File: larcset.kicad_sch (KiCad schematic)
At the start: 246 parts, among them J1 EAR, J2 ANT, J3 MIC, J4 KEY, J6 Barrel_Jack_Switch, J7 FRONT_PANEL, J8 Conn_01x02, K1 G5V-2, Q1 MMBT2222A, Q10 MMBT2222A, Q11 2N7002, Q12 2N7002, Q13 2N3904, Q14 MMBT2222A, Q15 MMBT2222A, Q16 2N7002, Q17 2N7002, Q18 MMBT2222A, Q19 2N3904, Q2 MMBT2222A, Q20 2N7002, Q21 2N7002, Q22 IRF510N, Q3 MMBT2222A, Q4 MMBT2222A, Q5 MMBT2222A, Q6 MMBT2222A, Q7 MMBT2222A, Q8 MMBT2222A, Q9 MMBT2222A, T1 TRIFILAR_XFRMR, T2 TRIFILAR_XFRMR, T3 TRIFILAR_XFRMR, U1 LM386, Y1 11.059M, Y2 11.059M, Y3 11.059M, Y4 11.059M, Y5 11.059M

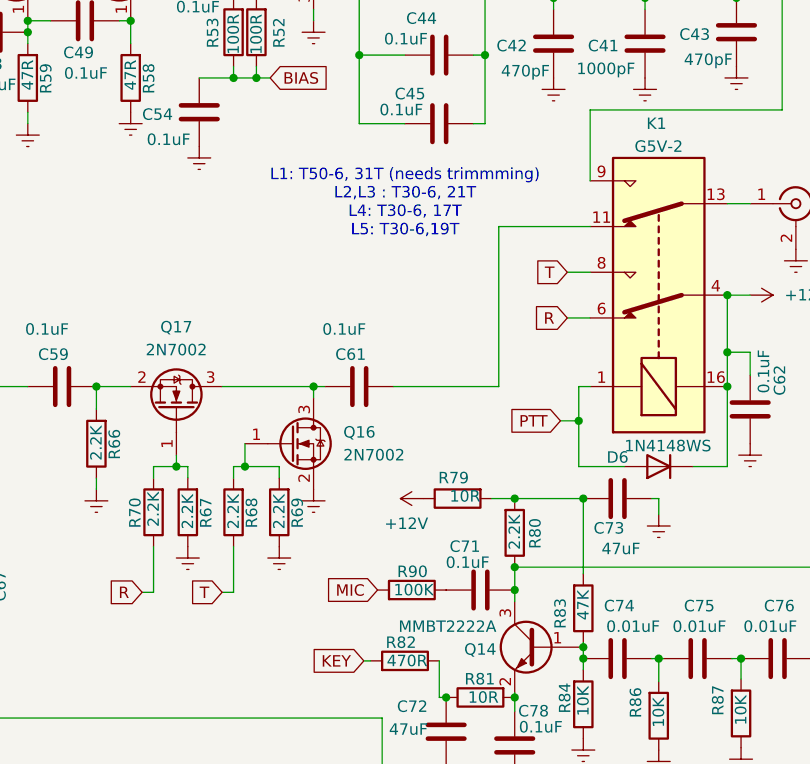
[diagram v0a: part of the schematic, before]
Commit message: Updated inductor values
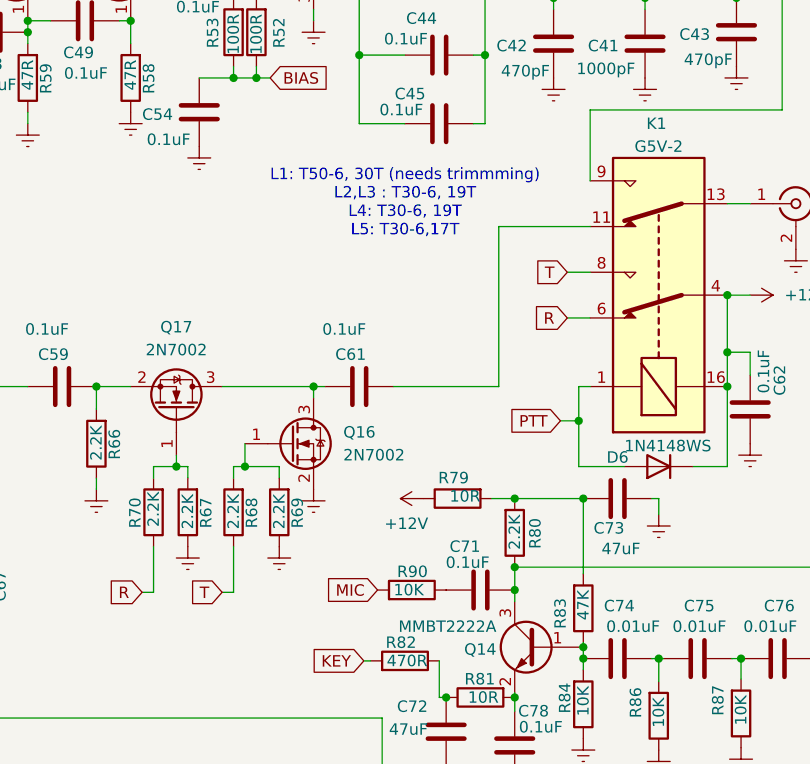
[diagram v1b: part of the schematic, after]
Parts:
- R90: value 100K -> 10K
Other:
- note added: "L1: T50-6, 30T (needs trimmming) L2,L3 : T30-6, 19T L4: T30-6, 19T L5: T30-6,17T"
- note removed: "L1: T50-6, 31T (needs trimmming) L2,L3 : T30-6, 21T L4: T30-6, 17T L5: T30-6,19T"
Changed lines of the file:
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@@
 		)
 	)
-	(text "L1: T50-6, 31T (needs trimmming)\nL2,L3 : T30-6, 21T\nL4: T30-6, 17T\nL5: T30-6,19T"
+	(text "L1: T50-6, 30T (needs trimmming)\nL2,L3 : T30-6, 19T\nL4: T30-6, 19T\nL5: T30-6,17T"
 		(exclude_from_sim no)
 		(at 237.49 60.96 0)
@@
 			)
 		)
-		(property "Value" "100K"
+		(property "Value" "10K"
 			(at 236.22 103.886 90)
 			(effects
